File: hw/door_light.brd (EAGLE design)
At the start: 32.2 x 34.6 mm, 28 parts, among them IC1 TINY13-20SSU, Q1 BSP250, T1 n-mosfet, T2 KP-3216P3C, U1 MC33063ADE4

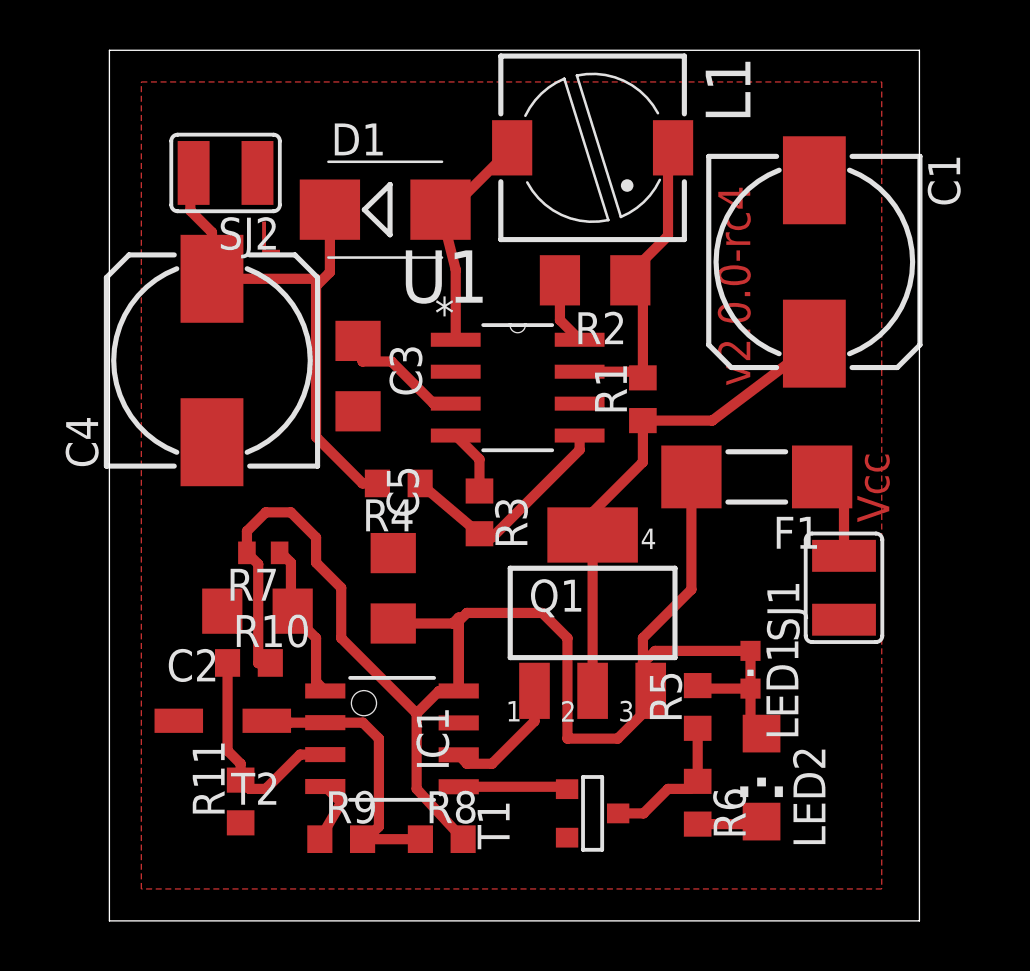
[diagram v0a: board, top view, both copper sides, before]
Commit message: fixed invalid path under LED1
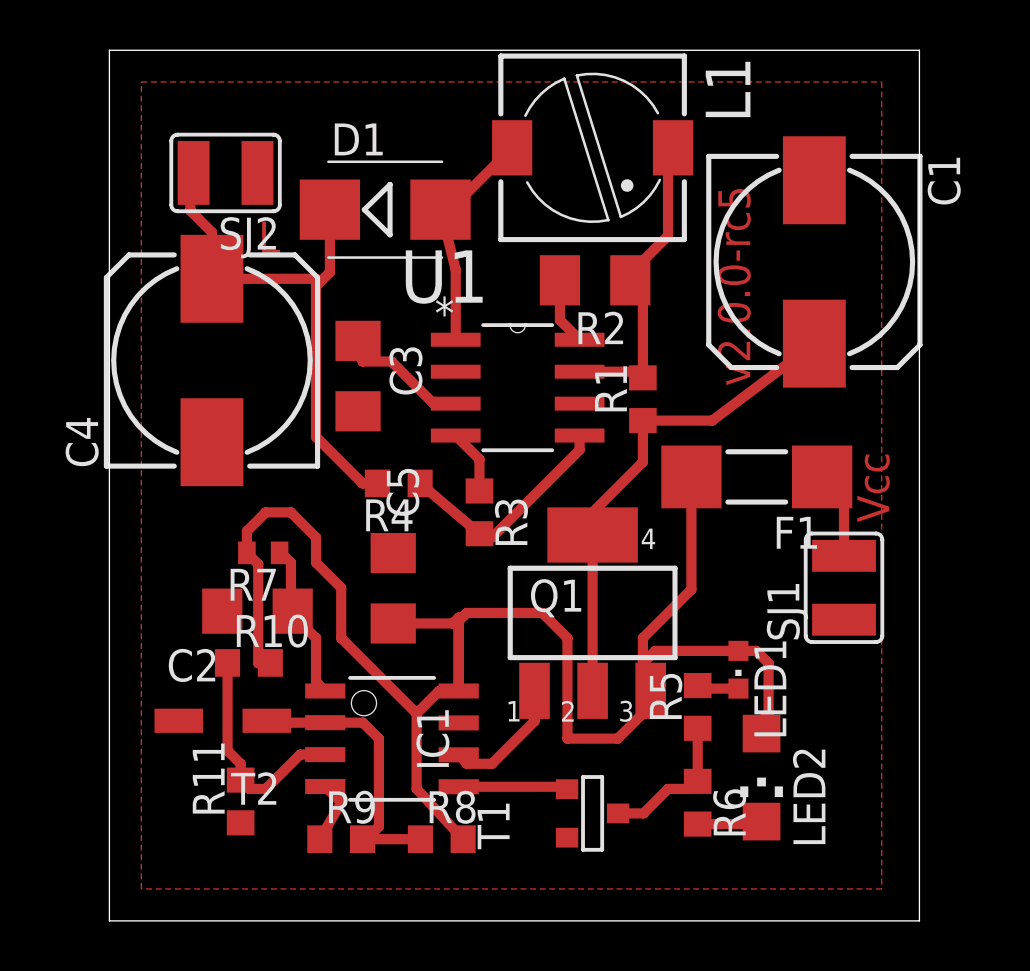
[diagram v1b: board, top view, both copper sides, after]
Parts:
- moved LED1 0.48 mm to (42.8, 49.7)
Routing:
- net +4.1V: track 65.2 -> 66.1 mm
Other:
- board text added: "v2.0.0-rc5"
- board text removed: "v2.0.0-rc4"
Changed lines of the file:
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@@
 <layer number="45" name="Holes" color="7" fill="1" visible="no" active="yes"/>
 <layer number="46" name="Milling" color="3" fill="1" visible="no" active="yes"/>
-<layer number="47" name="Measures" color="7" fill="1" visible="yes" active="yes"/>
+<layer number="47" name="Measures" color="7" fill="1" visible="no" active="yes"/>
 <layer number="48" name="Document" color="7" fill="1" visible="yes" active="yes"/>
 <layer number="49" name="Reference" color="7" fill="1" visible="yes" active="yes"/>
@@
 <text x="48.8" y="55.6" size="1.27" layer="1" rot="R90">Vcc</text>
 <text x="23.7" y="66.3" size="1.27" layer="1">L</text>
-<text x="42" y="69" size="1.27" layer="1" rot="R270">v2.0.0-rc4</text>
+<text x="42" y="69" size="1.27" layer="1" rot="R270">v2.0.0-rc5</text>
 </plain>
 <attributes>
@@
 <element name="R11" library="rcl" package="R0603" value="2.9kR" x="23" y="44.5" rot="R90"/>
 <element name="LED2" library="led" package="CHIPLED_1206" value="IR" x="43.72" y="45.45" rot="R180"/>
-<element name="LED1" library="led" package="CHIPLED_0603" value="RED" x="43.28" y="49.74" rot="R180"/>
+<element name="LED1" library="led" package="CHIPLED_0603" value="RED" x="42.8" y="49.74" rot="R180"/>
 <element name="R6" library="rcl" package="R0603" value="470R" x="41.18" y="44.45" rot="R270"/>
 <element name="R5" library="rcl" package="R0603" value="470R" x="41.18" y="48.26" rot="R90"/>
@@
 <wire x1="29.07" y1="51.58" x2="31.438" y2="51.58" width="0.4064" layer="1"/>
 <wire x1="31.438" y1="51.58" x2="31.674" y2="51.816" width="0.4064" layer="1"/>
-<wire x1="43.28" y1="50.49" x2="39.49" y2="50.49" width="0.4064" layer="1"/>
+<wire x1="42.8" y1="50.49" x2="39.49" y2="50.49" width="0.4064" layer="1"/>
 <wire x1="39.49" y1="50.49" x2="39" y2="50" width="0.4064" layer="1"/>
-<wire x1="43.28" y1="50.49" x2="43.28" y2="47.64" width="0.4064" layer="1"/>
 <wire x1="43.28" y1="47.64" x2="43.72" y2="47.2" width="0.4064" layer="1"/>
+<wire x1="42.8" y1="50.49" x2="43.51" y2="50.49" width="0.4064" layer="1"/>
+<wire x1="43.51" y1="50.49" x2="44" y2="50" width="0.4064" layer="1"/>
+<wire x1="43.28" y1="47.64" x2="43.64" y2="47.64" width="0.4064" layer="1"/>
+<wire x1="43.64" y1="47.64" x2="44" y2="48" width="0.4064" layer="1"/>
+<wire x1="44" y1="48" x2="44" y2="50" width="0.4064" layer="1"/>
 </signal>
 <signal name="N$10">
@@
 <contactref element="LED1" pad="C"/>
 <contactref element="R5" pad="2"/>
-<wire x1="43.28" y1="48.99" x2="41.3" y2="48.99" width="0.4064" layer="1"/>
+<wire x1="42.8" y1="48.99" x2="41.3" y2="48.99" width="0.4064" layer="1"/>
 <wire x1="41.3" y1="48.99" x2="41.18" y2="49.11" width="0.4064" layer="1"/>
 </signal>

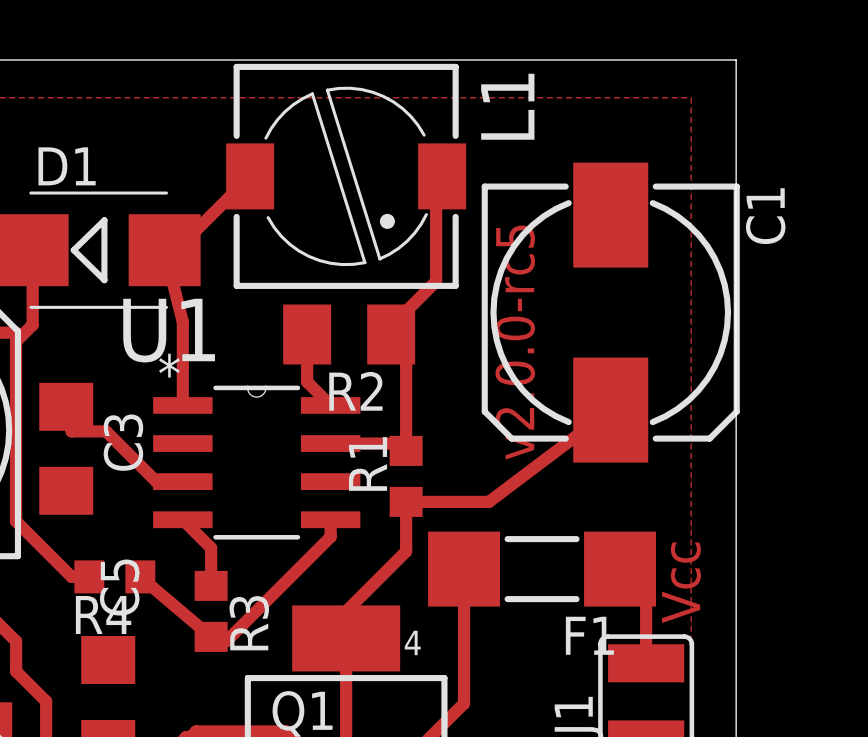
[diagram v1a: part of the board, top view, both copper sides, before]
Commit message: 180R size changed from 1206 to 603
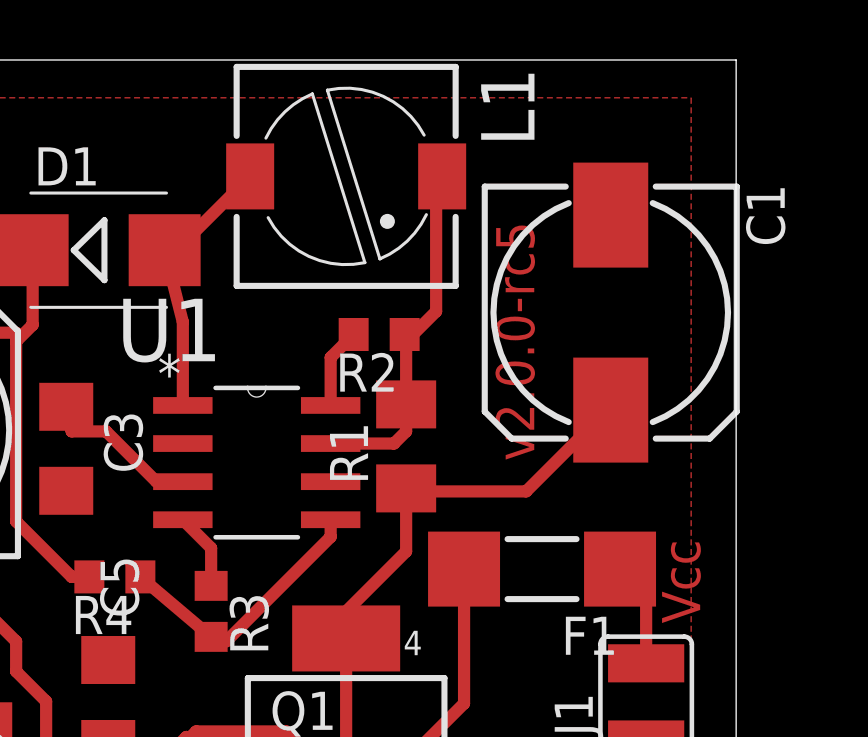
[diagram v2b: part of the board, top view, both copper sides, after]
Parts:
- R1: device rcl:R0603 -> rcl:M1206
- R2: device rcl:M1206 -> rcl:R0603
- moved R1 1.00 mm to (39.0, 61.5)
- moved R2 1.00 mm to (38.1, 65.2)
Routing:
- net N$16: track 12.7 -> 11.9 mm
- net N$3: track 19.4 -> 20.0 mm
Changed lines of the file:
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@@
 <element name="C4" library="rcl" package="153CLV-0810" value="100uF" x="21.86" y="62.04" rot="R90"/>
 <element name="L1" library="rcl" package="PIS2816" value="150uH" x="37" y="70.5" rot="R270"/>
-<element name="R2" library="rcl" package="M1206" value="180R" x="37.1" y="65.23" rot="R180"/>
-<element name="R1" library="rcl" package="R0603" value="0.22R" x="39" y="60.5" rot="R90"/>
+<element name="R2" library="rcl" package="R0603" value="180R" x="38.1" y="65.23" rot="R180"/>
+<element name="R1" library="rcl" package="M1206" value="0.22R" x="39" y="61.5" rot="R90"/>
 <element name="R4" library="rcl" package="R0603" value="24kR" x="29.29" y="57.15" rot="R180"/>
 <element name="R3" library="rcl" package="R0603" value="2.7kR" x="32.5" y="56" rot="R270"/>
@@
 <contactref element="U1" pad="8"/>
 <contactref element="R2" pad="2"/>
-<wire x1="35.7" y1="65.23" x2="35.7" y2="63.6488" width="0.4064" layer="1"/>
-<wire x1="35.7" y1="63.6488" x2="36.4838" y2="62.865" width="0.4064" layer="1"/>
+<wire x1="36.4838" y1="62.865" x2="36.4838" y2="64.4638" width="0.4064" layer="1"/>
+<wire x1="36.4838" y1="64.4638" x2="37.25" y2="65.23" width="0.4064" layer="1"/>
 </signal>
 <signal name="N$16">
@@
 <contactref element="U1" pad="7"/>
 <contactref element="R1" pad="2"/>
-<wire x1="36.4838" y1="61.595" x2="38.554571875" y2="61.595" width="0.4064" layer="1"/>
-<wire x1="39" y1="61.35" x2="39" y2="64.73" width="0.4064" layer="1"/>
-<wire x1="39" y1="64.73" x2="38.5" y2="65.23" width="0.4064" layer="1"/>
-<wire x1="38.5" y1="65.23" x2="38.5" y2="65.5" width="0.4064" layer="1"/>
-<wire x1="38.5" y1="65.5" x2="40" y2="67" width="0.4064" layer="1"/>
-<wire x1="40" y1="67" x2="40" y2="70.3" width="0.4064" layer="1"/>
+<wire x1="36.4838" y1="61.595" x2="38.595" y2="61.595" width="0.4064" layer="1"/>
+<wire x1="40" y1="66" x2="40" y2="70.3" width="0.4064" layer="1"/>
 <wire x1="40" y1="70.3" x2="40.2" y2="70.5" width="0.4064" layer="1"/>
-<wire x1="39" y1="61.35" x2="38.799571875" y2="61.35" width="0.4064" layer="1"/>
-<wire x1="38.799571875" y1="61.35" x2="38.554571875" y2="61.595" width="0.4064" layer="1"/>
+<wire x1="38.595" y1="61.595" x2="39" y2="62" width="0.4064" layer="1"/>
+<wire x1="39" y1="62" x2="39" y2="62.9" width="0.4064" layer="1"/>
+<wire x1="39" y1="62.9" x2="39" y2="65.18" width="0.4064" layer="1"/>
+<wire x1="39" y1="65.18" x2="38.95" y2="65.23" width="0.4064" layer="1"/>
+<wire x1="38.95" y1="65.23" x2="39.23" y2="65.23" width="0.4064" layer="1"/>
+<wire x1="39.23" y1="65.23" x2="40" y2="66" width="0.4064" layer="1"/>
 </signal>
 <signal name="N$18">
@@
 <contactref element="R1" pad="1"/>
 <contactref element="C1" pad="+"/>
-<wire x1="39" y1="59.65" x2="41.76" y2="59.65" width="0.4064" layer="1"/>
-<wire x1="41.76" y1="59.65" x2="45.82" y2="62.71" width="0.4064" layer="1"/>
 <contactref element="Q1" pad="2"/>
 <contactref element="Q1" pad="4"/>
 <wire x1="37" y1="55.099" x2="37" y2="56" width="0.4064" layer="1"/>
 <wire x1="37" y1="56" x2="39" y2="58" width="0.4064" layer="1"/>
-<wire x1="39" y1="58" x2="39" y2="59.65" width="0.4064" layer="1"/>
+<wire x1="39" y1="58" x2="39" y2="60.1" width="0.4064" layer="1"/>
 <wire x1="37" y1="48.9012" x2="37" y2="55.099" width="0.4064" layer="1"/>
+<wire x1="45.82" y1="62.71" x2="45.71" y2="62.71" width="0.4064" layer="1"/>
+<wire x1="45.71" y1="62.71" x2="43" y2="60" width="0.4064" layer="1"/>
+<wire x1="43" y1="60" x2="39.1" y2="60" width="0.4064" layer="1"/>
+<wire x1="39.1" y1="60" x2="39" y2="60.1" width="0.4064" layer="1"/>
 </signal>
 <signal name="VCC">

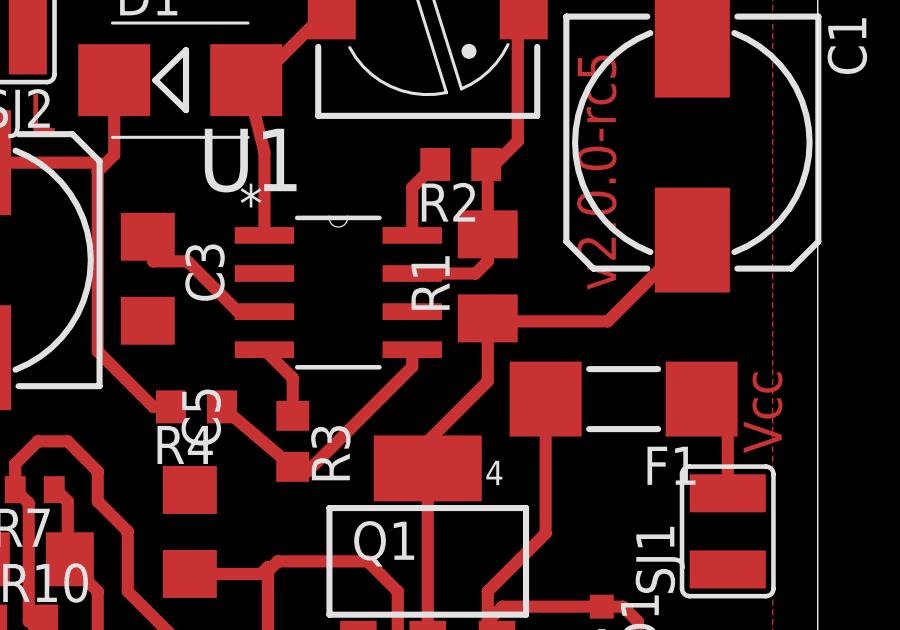
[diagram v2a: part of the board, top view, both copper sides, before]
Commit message: DC/DC converter is nowe powered...
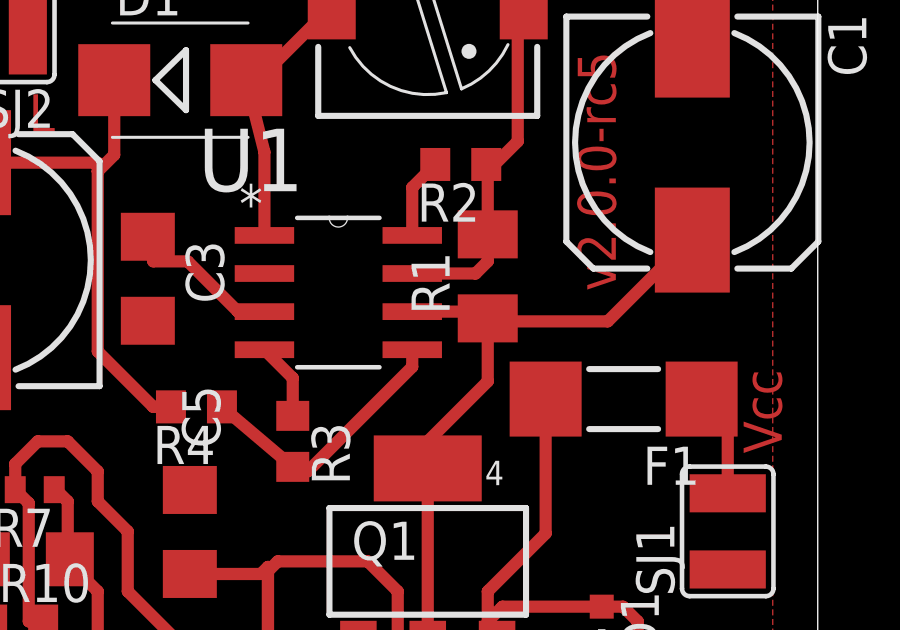
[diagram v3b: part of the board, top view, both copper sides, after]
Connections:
- removed net VCC: U1.6
- net N$3: now also U1.6
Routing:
- net N$3: track 20.0 -> 22.6 mm
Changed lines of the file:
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@@
 <wire x1="43" y1="60" x2="39.1" y2="60" width="0.4064" layer="1"/>
 <wire x1="39.1" y1="60" x2="39" y2="60.1" width="0.4064" layer="1"/>
-</signal>
-<signal name="VCC">
 <contactref element="U1" pad="6"/>
+<wire x1="36.4838" y1="60.325" x2="38.775" y2="60.325" width="0.4064" layer="1"/>
+<wire x1="38.775" y1="60.325" x2="39" y2="60.1" width="0.4064" layer="1"/>
 </signal>
 </signals>

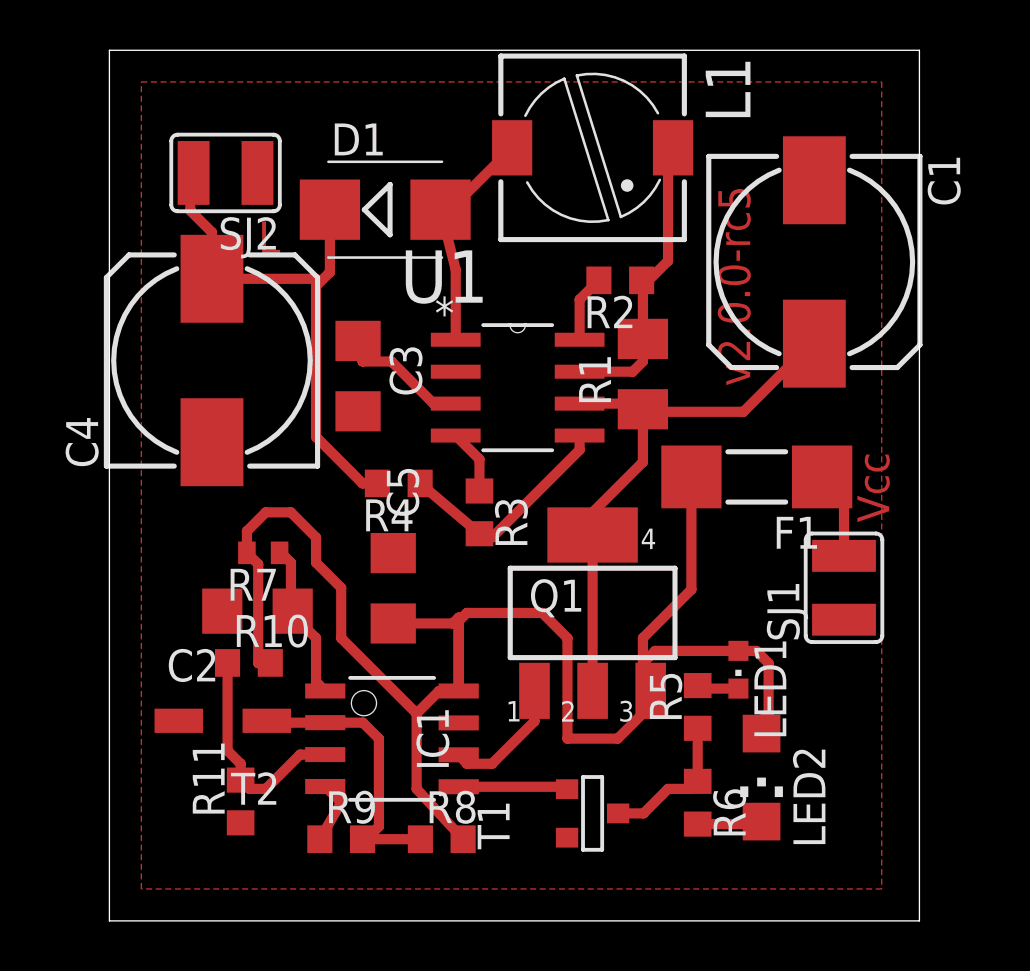
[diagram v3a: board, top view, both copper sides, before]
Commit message: added missing R to GND from transistors' gates
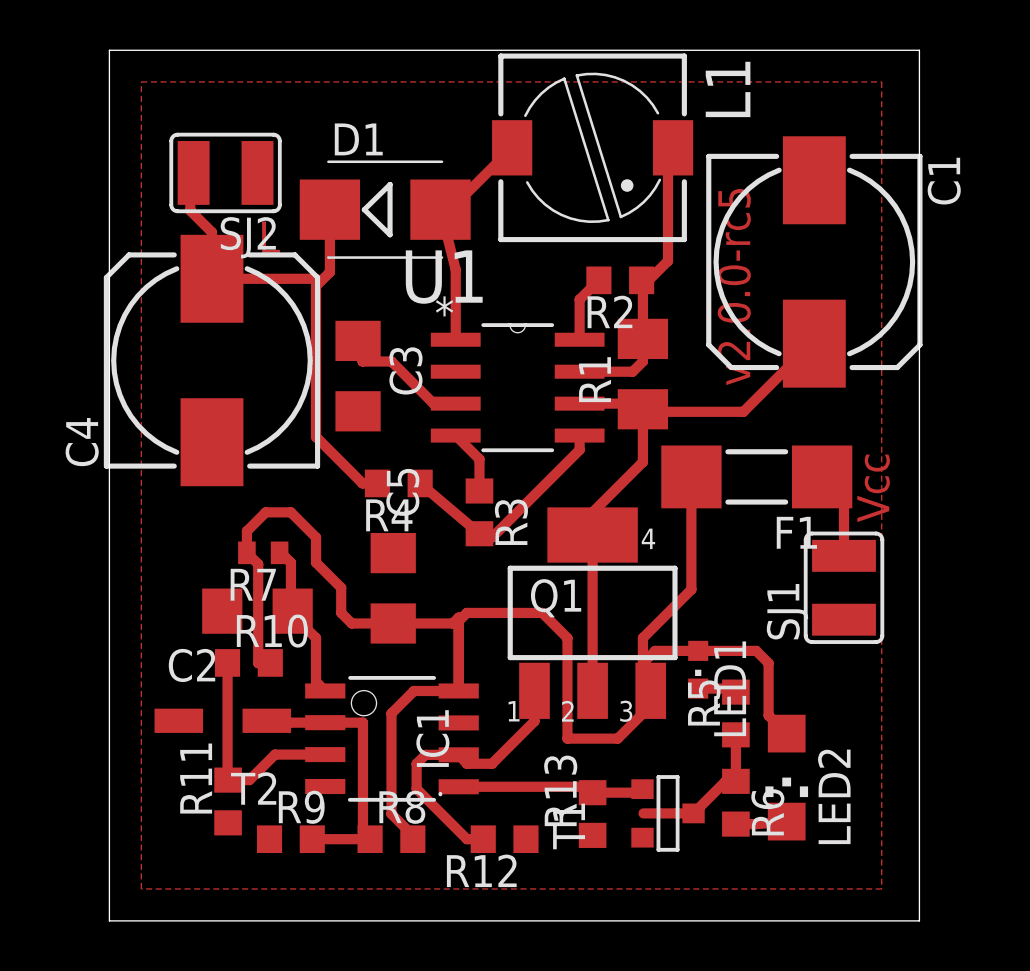
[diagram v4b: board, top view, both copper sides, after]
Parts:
- added R12, R13: 100kR, rcl:R0603
- moved T1 3.00 mm to (40.0, 44.0)
- moved R8 2.00 mm to (29.0, 43.0)
- moved R9 2.00 mm to (25.0, 43.0)
- moved LED1 1.60 mm to (41.2, 49.7)
- moved R5 1.54 mm to (42.7, 48.0)
- moved R6 1.52 mm to (42.7, 44.5)
- moved LED2 1.00 mm to (44.7, 45.5)
- moved R11 0.50 mm to (22.5, 44.5)
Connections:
- net 0V: now also R12.1, R13.1
- net N$13: now also R12.2
- net N$14: now also R13.2
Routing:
- net N$13: track 5.08 -> 11.4 mm
- net N$14: track 4.35 -> 7.47 mm
- net +4.1V: track 66.1 -> 63.3 mm
- net 0V: track 5.18 -> 2.60 mm
- net N$2: track 2.56 -> 2.02 mm
